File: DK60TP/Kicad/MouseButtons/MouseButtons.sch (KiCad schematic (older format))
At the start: 9 parts, among them K1 K43, K2 K43, K3 K44, K4 K45, K5 K45, P1 CONN_01X04

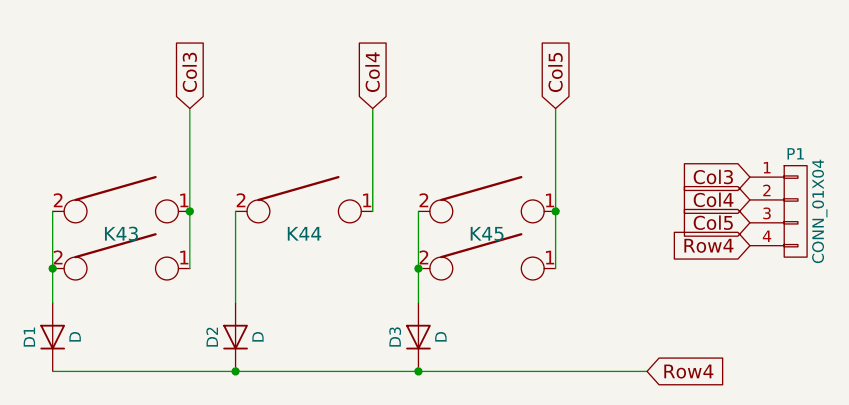
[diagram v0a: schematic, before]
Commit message: - DK60TP: reducing quantity of VIAs
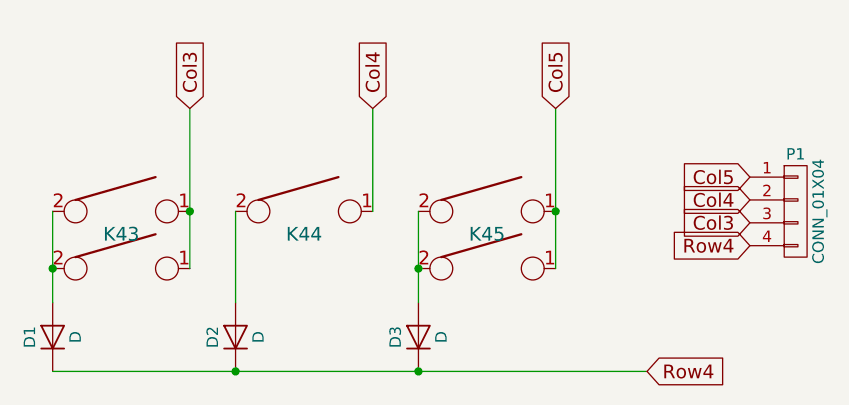
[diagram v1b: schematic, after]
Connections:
- net Col3: now also P1.3 (P3); no longer P1.1 (P1)
- net Col5: now also P1.1 (P1); no longer P1.3 (P3)
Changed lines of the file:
@@
 LIBS:mkl27z256vfm4
 LIBS:Trackpad
+LIBS:MouseButtons-cache
 EELAYER 25 0
 EELAYER END
@@
 Text GLabel 4750 1450 0    60   Input ~ 0
 Row4
-Text GLabel 4750 1350 0    60   Input ~ 0
+Text GLabel 4750 1150 0    60   Input ~ 0
 Col5
 Text GLabel 4750 1250 0    60   Input ~ 0
 Col4
-Text GLabel 4750 1150 0    60   Input ~ 0
+Text GLabel 4750 1350 0    60   Input ~ 0
 Col3
 $EndSCHEMATC
